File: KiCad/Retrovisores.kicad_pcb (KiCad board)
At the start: 2 copper layers, 64 parts, among them J1 Conn_01x02_Pin, J2 DE9_Pins, J4 DE9_Pins, J5 Conn_01x02_Pin, J6 Conn_01x02_Pin, J7 Conn_01x02_Pin, J8 Conn_PIC_ICSP_ICD, Q14 AO3400A, Q15 AO3401A, Q16 AO3400A, Q17 AO3401A, Q18 AO3400A, Q19 AO3401A, Q20 AO3400A, Q21 AO3401A, Q22 AO3400A, Q23 AO3401A, Q24 AO3400A, Q25 AO3401A, Q27 AO3400A, SW1 SW_Push, SW2 SW_Push, SW3 SW_Push, SW4 SW_Push, SW6 SW_Nidec_CAS-120A1, U1 SHTC3, U2 SN65HVD232, U4 LT1117-3.3, U5 TSR3-2450N, U6 VL53L1CXV0FY1, U7 PIC32MX250F128D-IPT, Y1 Crystal

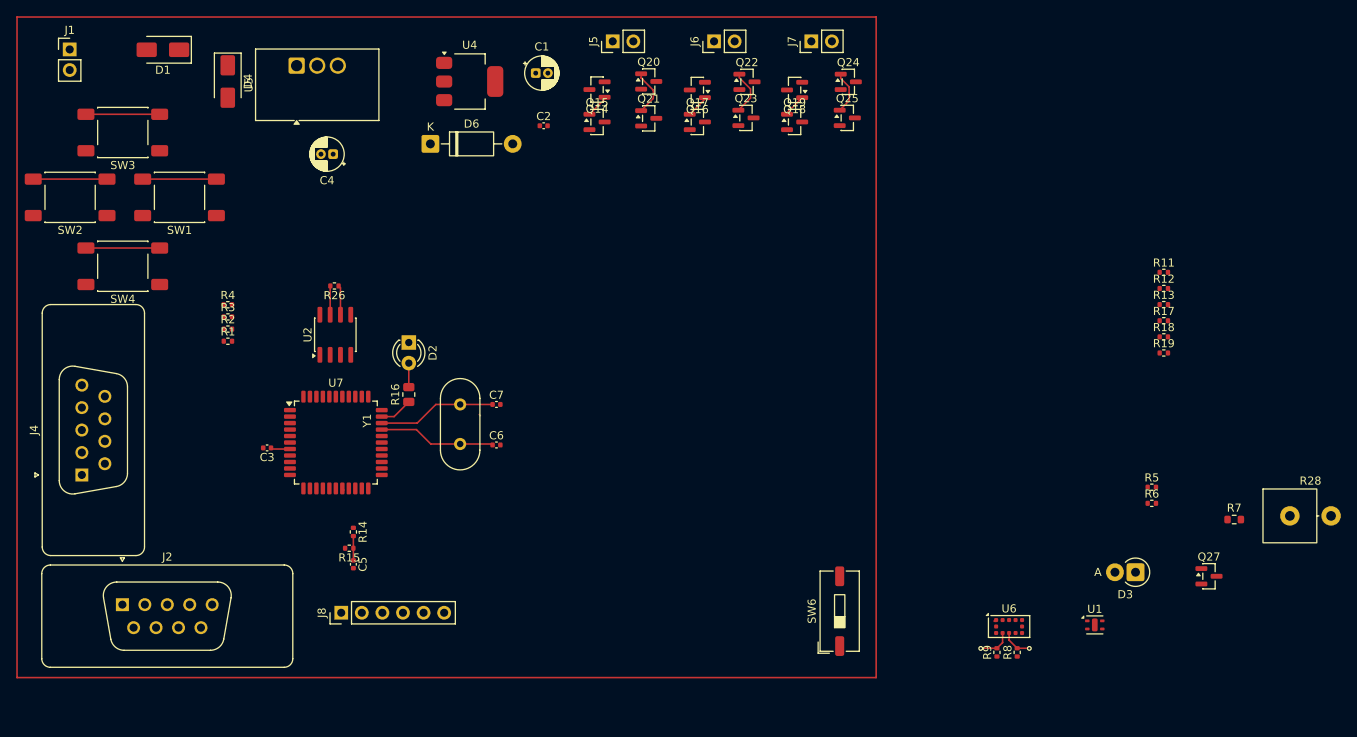
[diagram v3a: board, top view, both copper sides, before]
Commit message: cambiado layout general
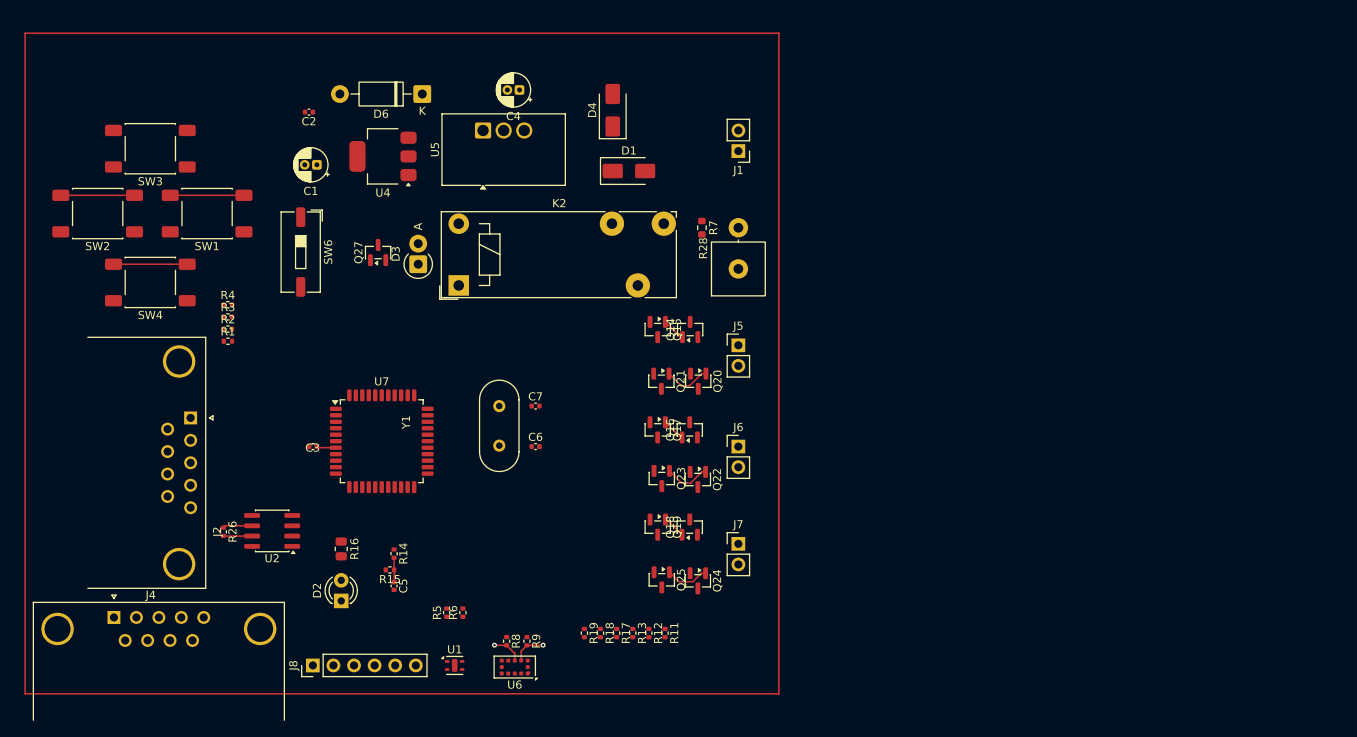
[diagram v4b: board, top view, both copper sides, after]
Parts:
- added K2: Relay_SPDT, Relay_THT:Relay_1-Form-C_Schrack-RYII_RM3.2mm, F.Cu at (139.5, 53.1)
- J2, J4: footprint Connector_Dsub:DSUB-9_Pins_Vertical_P2.77x2.84mm -> Connector_Dsub:DSUB-9_Pins_Horizontal_P2.77x2.84mm_EdgePinOffset9.90mm_Housed_MountingHolesOffset11.32mm
- moved Q27 110.0 mm to (129.6, 49.1), turned to 90 degrees
- moved D3 96.3 mm to (134.5, 50.5), turned to 90 degrees
- moved R5 88.4 mm to (138.0, 93.5), turned to 90 degrees
- moved R6 86.1 mm to (140.0, 93.5), turned to 90 degrees
- moved J1 83.4 mm to (174.0, 36.5), turned to 180 degrees
- moved SW6 79.9 mm to (120.0, 49.0), turned to -90 degrees
- moved R19 79.4 mm to (155.0, 96.0), turned to -90 degrees
- moved U1 79.1 mm to (139.0, 100.0)
- moved R18 78.5 mm to (157.0, 96.0), turned to -90 degrees
- moved R17 77.7 mm to (159.0, 96.0), turned to -90 degrees
- moved R13 77.0 mm to (161.0, 96.0), turned to -90 degrees
- moved R12 76.4 mm to (163.0, 96.0), turned to -90 degrees
- moved R11 75.9 mm to (164.9, 96.0), turned to -90 degrees
- moved R7 74.9 mm to (169.5, 46.0), turned to -90 degrees
- moved R28 74.6 mm to (174.0, 51.1), turned to 90 degrees
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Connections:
- R16 pad 1: Net-(U7-RA8) -> Net-(U7-RA10)
- U7 pad 1: DI2C -> R
- U7 pad 11: OP//CL -> RCAN
- U7 pad 12: SDL1 -> Net-(U7-RA10)
- U7 pad 2: R -> L
- U7 pad 25: FCR -> KLKI2C
- U7 pad 26: FCL -> DI2C
- U7 pad 3: L -> U
- U7 pad 32: Net-(U7-RA8) -> unconnected-(U7-RA8-Pad32)
- U7 pad 33: RCAN -> unconnected-(U7-RB4-Pad33)
- U7 pad 4: U -> D
- U7 pad 41: DCAN -> unconnected-(U7-RB5-Pad41)
- U7 pad 43: RX -> unconnected-(U7-RB7-Pad43)
- U7 pad 44: KLKI2C -> unconnected-(U7-RB8-Pad44)
- U7 pad 5: D -> RX
- U7 pad 8: HEAT -> TX
- U7 pad 9: TX -> DCAN
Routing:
- net OSC2: track 14.6 -> 0.00 mm
- net OSC1: track 14.5 -> 0.17 mm
- net U: track 9.10 -> 0.00 mm
- net Net-(U7-RA8): track 4.09 -> 0.00 mm
- net Net-(D2-A): track 2.96 -> 0.00 mm

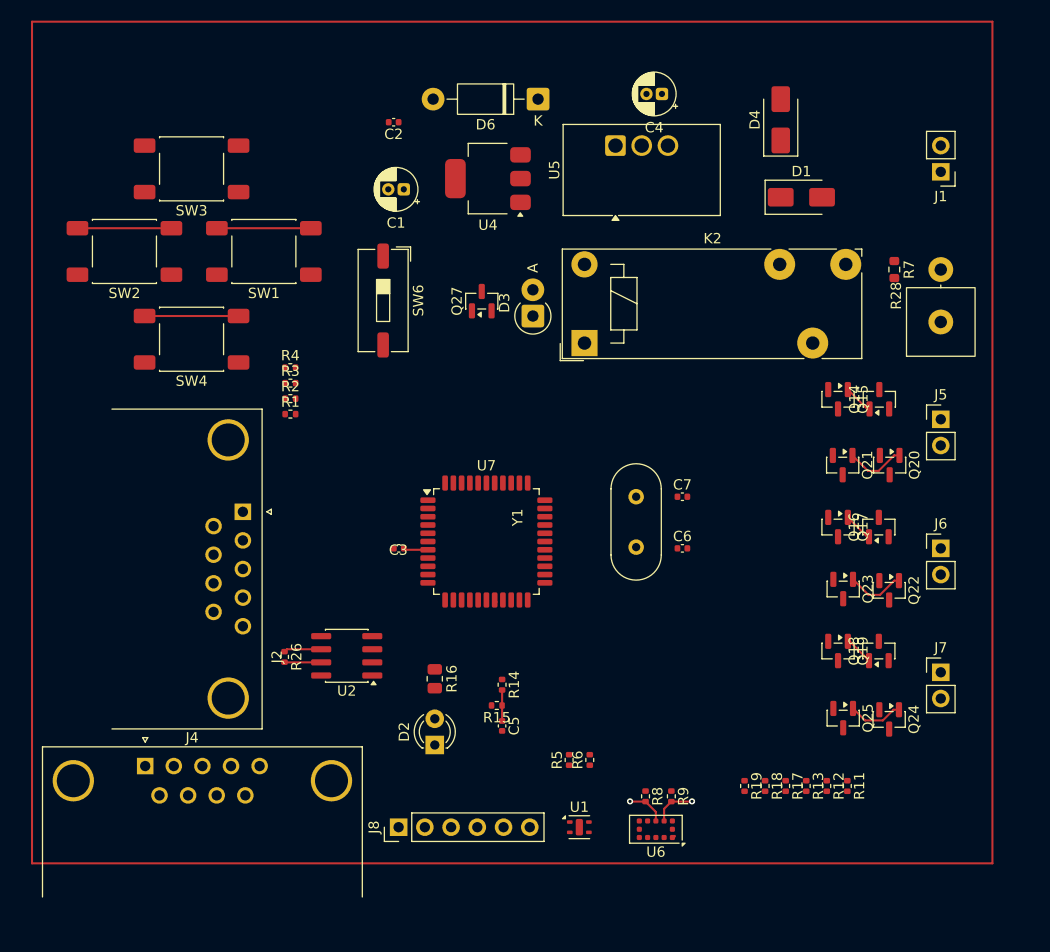
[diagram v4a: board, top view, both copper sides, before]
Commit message: terminado placement (reorganizado pines del micro y añadido cambios de sensores/calefactor por conectores)
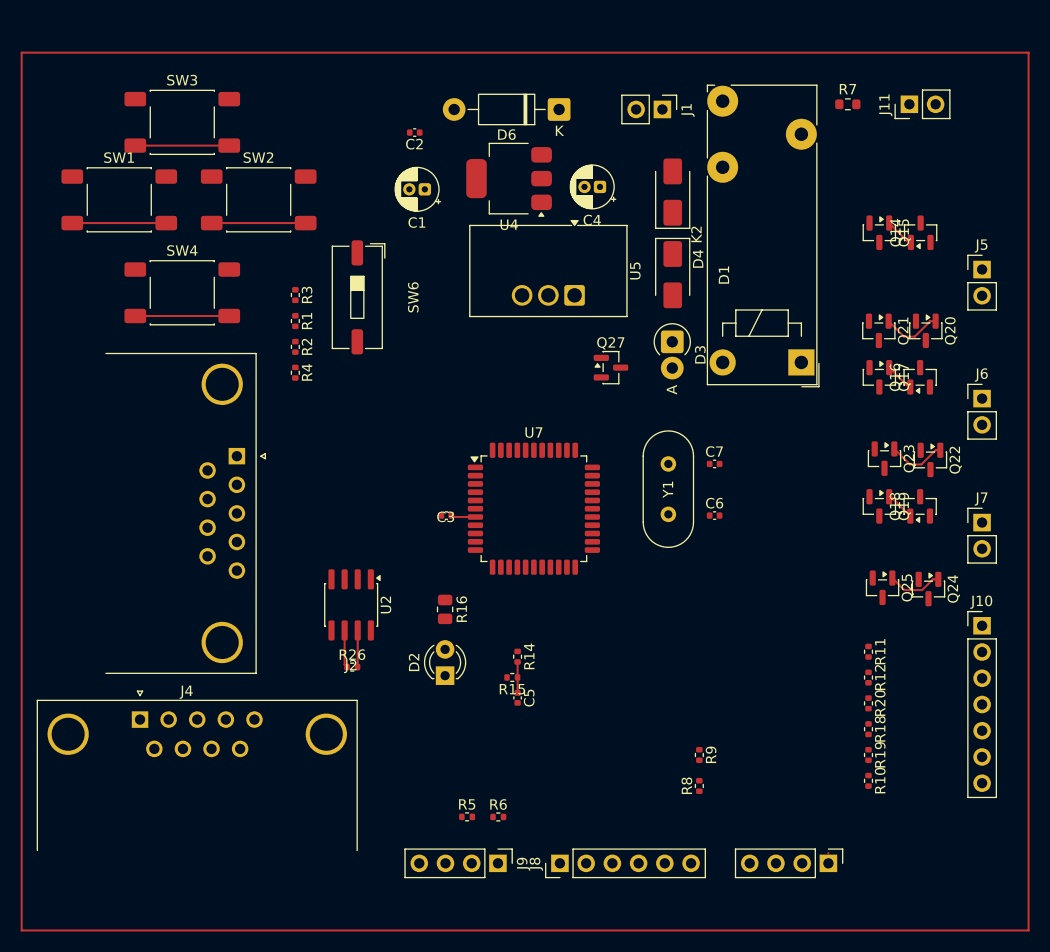
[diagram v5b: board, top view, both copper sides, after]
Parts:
- removed R13, R17: R, Resistor_SMD:R_0402_1005Metric
- removed R28: Heater, Resistor_THT:R_Axial_Power_L20.0mm_W6.4mm_P5.08mm_Vertical
- removed U1: SHTC3, Sensor_Humidity:Sensirion_DFN-4-1EP_2x2mm_P1mm_EP0.7x1.6mm
- removed U6: VL53L1CXV0FY1, Sensor_Distance:ST_VL53L1x
- added J10: Conn_01x07_Pin, Connector_PinHeader_2.54mm:PinHeader_1x07_P2.54mm_Vertical, F.Cu at (178.0, 80.5)
- added J11: Conn_01x02_Pin, Connector_PinHeader_2.54mm:PinHeader_1x02_P2.54mm_Vertical, F.Cu at (171.0, 30.0)
- added J3: Conn_01x04_Pin, Connector_PinHeader_2.54mm:PinHeader_1x04_P2.54mm_Vertical, F.Cu at (163.1, 103.5)
- added J9: Conn_01x04_Pin, Connector_PinHeader_2.54mm:PinHeader_1x04_P2.54mm_Vertical, F.Cu at (131.1, 103.5)
- added R10: R, Resistor_SMD:R_0402_1005Metric, F.Cu at (167.0, 95.5)
- added R20: R, Resistor_SMD:R_0402_1005Metric, F.Cu at (167.0, 88.0)
- moved J1 27.6 mm to (147.0, 30.5), turned to -90 degrees
- moved K2 21.1 mm to (160.5, 55.0), turned to 90 degrees
- moved D4 18.3 mm to (148.0, 46.5), turned to -90 degrees
- moved R7 16.6 mm to (165.0, 30.0), turned to 0 degrees
- moved Q14 16.6 mm to (172.1, 42.4)
- moved Q15 16.6 mm to (168.1, 42.4)
- moved J8 16.0 mm to (137.1, 103.5)
- moved J5 15.0 mm to (178.0, 46.0)
- moved J6 15.0 mm to (178.0, 58.5)
- moved J7 15.0 mm to (178.0, 70.5)
- moved Q16 15.0 mm to (172.0, 56.4)
- moved Q17 15.0 mm to (168.1, 56.4)
- moved U5 15.0 mm to (138.5, 48.5), turned to -90 degrees
- moved SW1 14.9 mm to (94.5, 39.2), turned to 0 degrees
- moved Q18 14.6 mm to (172.0, 68.9)
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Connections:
- R18 pad 1: FC5 -> FCU
- R19 pad 1: FC6 -> FC5
- U7 pad 13: CL -> unconnected-(U7-RA7-Pad13)
- U7 pad 14: unconnected-(U7-RB14-Pad14) -> SCL
- U7 pad 15: unconnected-(U7-RB15-Pad15) -> SDA
- U7 pad 19: SDR1 -> PGD
- U7 pad 20: SDU1 -> PGC
- U7 pad 21: PGD -> DI2C
- U7 pad 22: PGC -> KLKI2C
- U7 pad 23: SCL -> FC6
- U7 pad 24: SDA -> FC5
- U7 pad 25: KLKI2C -> FCU
- U7 pad 26: DI2C -> FCD
- U7 pad 27: FCD -> FCL
- U7 pad 32: unconnected-(U7-RA8-Pad32) -> FCR
- U7 pad 33: unconnected-(U7-RB4-Pad33) -> CL
- U7 pad 36: FCU -> SDU1
- U7 pad 37: FC5 -> SDL1
- U7 pad 38: FC6 -> SDR1
- U7 pad 43: unconnected-(U7-RB7-Pad43) -> HEAT
- U7 pad 44: unconnected-(U7-RB8-Pad44) -> OP//CL
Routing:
- net U: track 0.00 -> 9.10 mm
- net KLKI2C: track 4.18 -> 0.00 mm, vias 1 -> 0
- net DI2C: track 3.80 -> 0.00 mm, vias 1 -> 0
- net R: track 9.78 -> 9.10 mm

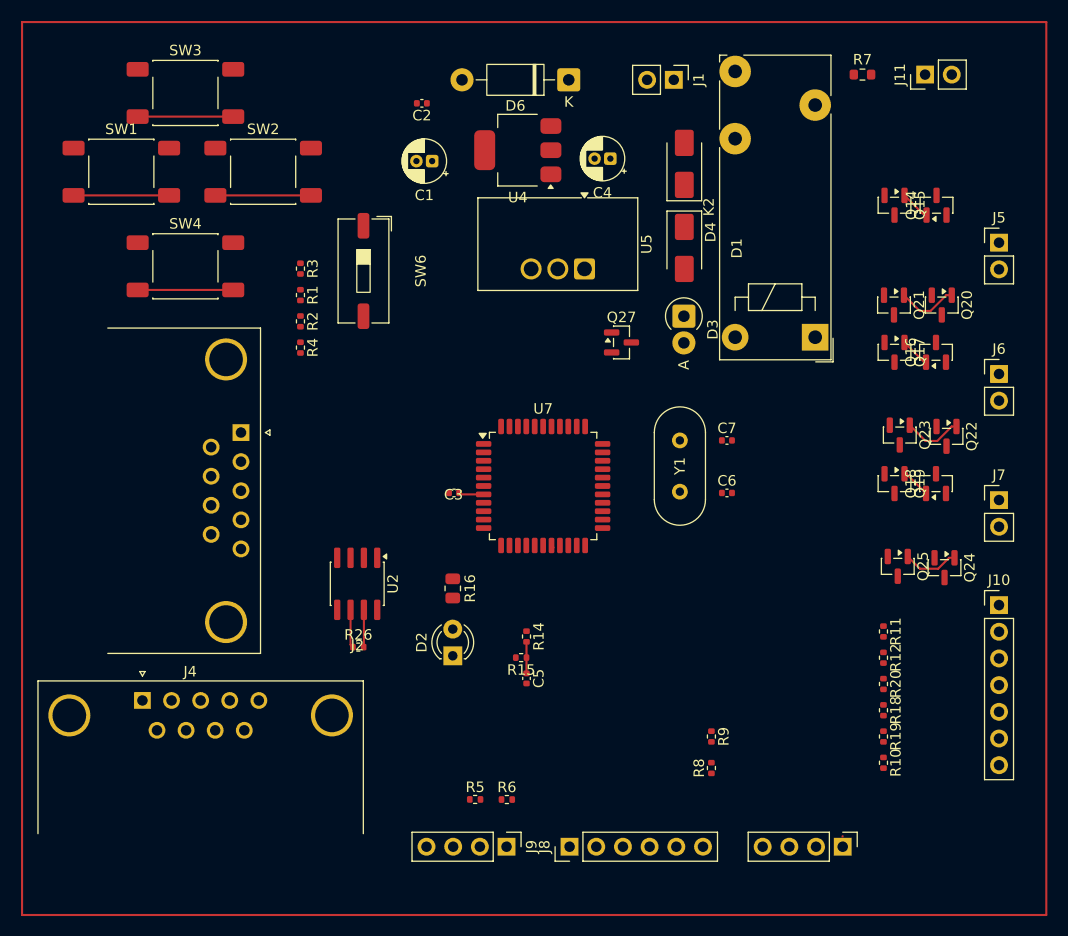
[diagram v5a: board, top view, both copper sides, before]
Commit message: routing V1.0 y recolocado algunos pines del Micro para eliminar islas//malas conexiones que no habia previsto
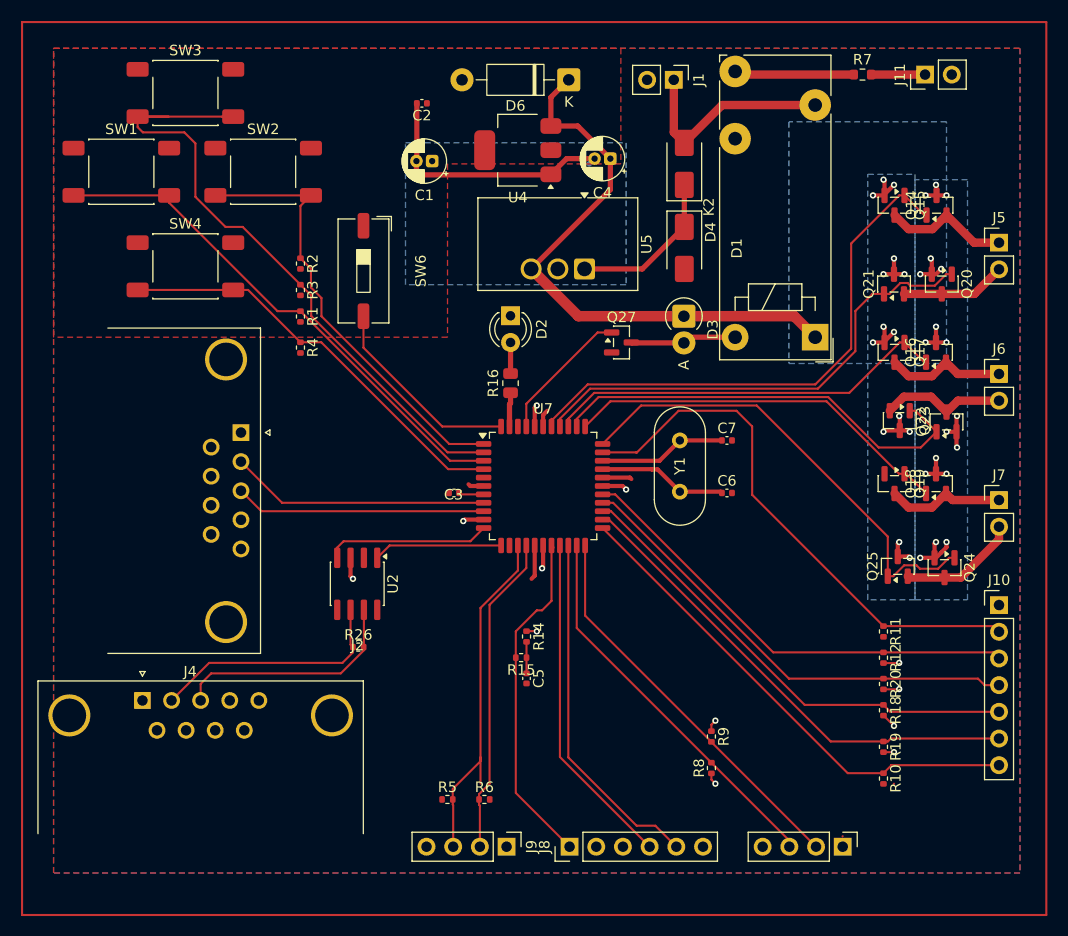
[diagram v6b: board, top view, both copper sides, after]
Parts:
- moved D2 32.8 mm to (131.5, 53.0), turned to -90 degrees
- moved R16 20.3 mm to (131.5, 59.4), turned to 90 degrees
- moved R2 5.50 mm to (111.5, 48.0)
- moved R5 2.64 mm to (125.5, 99.0)
- moved R6 2.14 mm to (129.0, 99.0)
- moved R1 2.04 mm to (111.5, 53.0)
- moved R3 2.04 mm to (111.5, 50.5)
- moved Q20 2.00 mm to (172.6, 49.9)
- moved Q21 2.00 mm to (168.0, 49.9), turned to 90 degrees
- moved R10 1.50 mm to (167.0, 97.0)
- moved Q22 1.38 mm to (173.0, 63.1), turned to 90 degrees
- moved Q23 1.38 mm to (168.6, 62.9)
- moved R19 0.98 mm to (167.0, 94.0)
- turned Q25 to 90 degrees
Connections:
- D2 pad 1: GND -> unconnected-(D2-K-Pad1)
- Q14 pad 3: 5VR -> 5V
- Q16 pad 3: 5VR -> 5V
- Q20 pad 2: 5VR -> 5V
- Q22 pad 2: 5VR -> 5V
- R16 pad 1: Net-(U7-RA10) -> Net-(U7-RB7)
- U7 pad 1: R -> L
- U7 pad 11: RCAN -> DCAN
- U7 pad 12: Net-(U7-RA10) -> RCAN
- U7 pad 2: L -> U
- U7 pad 3: U -> R
- U7 pad 41: unconnected-(U7-RB5-Pad41) -> HEAT
- U7 pad 43: HEAT -> Net-(U7-RB7)
- U7 pad 5: RX -> unconnected-(U7-RC9-Pad5)
- U7 pad 8: TX -> RX
- U7 pad 9: DCAN -> TX
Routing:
- net 5V: track 0.00 -> 78.2 mm, vias 0 -> 18
- net GND: track 0.03 -> 57.8 mm, vias 0 -> 18
- net U: track 9.10 -> 64.0 mm
- net FCR: track 0.00 -> 51.9 mm
- net SDR1: track 2.88 -> 52.5 mm
- net FC6: track 0.00 -> 47.7 mm
- net FC5: track 0.00 -> 46.6 mm
- net FCU: track 0.00 -> 45.6 mm
- net FCD: track 0.00 -> 44.9 mm
- net FCL: track 0.00 -> 44.2 mm
- net R: track 9.10 -> 49.9 mm
- net SDL1: track 5.79 -> 46.2 mm
- net CL: track 5.36 -> 45.0 mm
- net KLKI2C: track 0.00 -> 37.8 mm
- net DI2C: track 0.00 -> 37.1 mm
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- added copper zone on B.Cu, net 5V
- added copper zone on B.Cu, net GND
- added copper zone on F.Cu, net GND
- added copper zone on B.Cu, net VCC
- added copper zone on F.Cu, net VCC
